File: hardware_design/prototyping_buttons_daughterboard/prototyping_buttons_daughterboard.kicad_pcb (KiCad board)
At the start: 2 copper layers, 80 x 30.5 mm, 10 parts, among them J1 Conn_02x10_Counter_Clockwise, J2 Conn_02x10_Counter_Clockwise

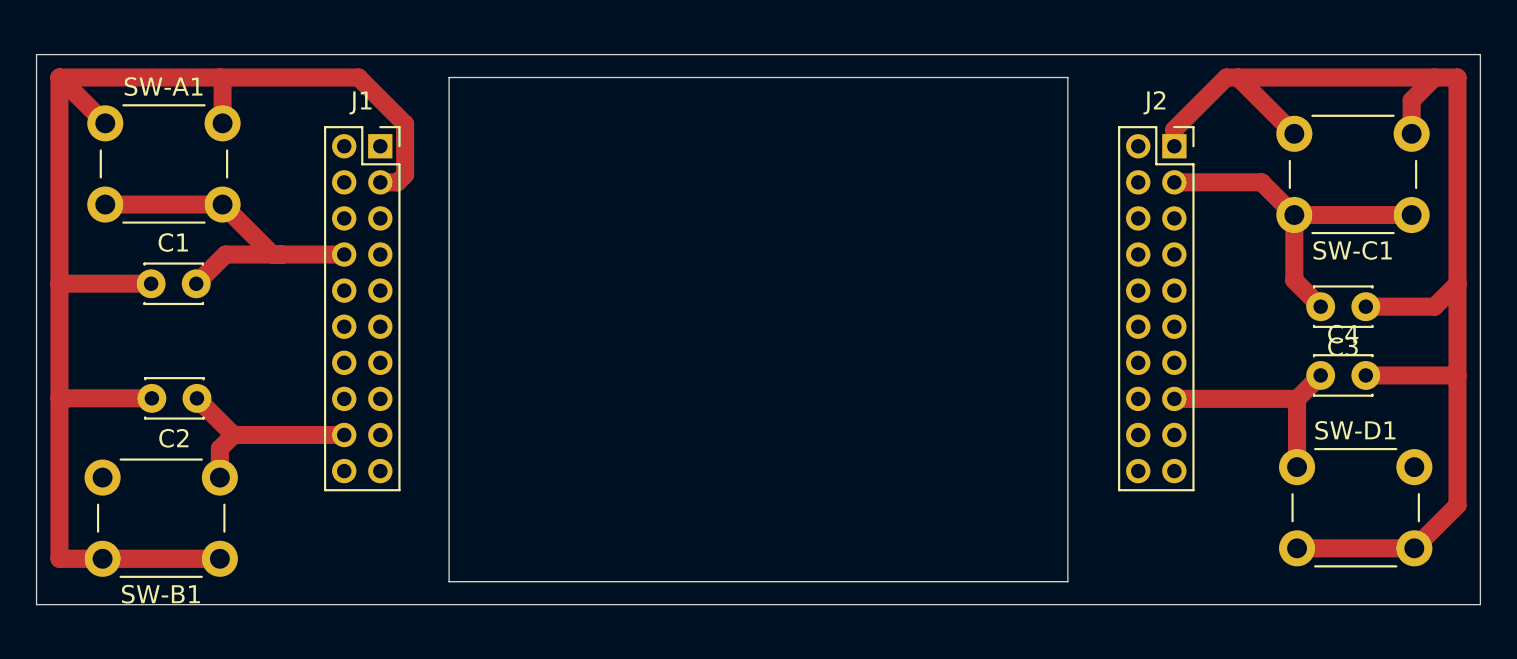
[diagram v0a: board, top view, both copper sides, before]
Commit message: Commit fixes issues with board design as raised in #3.
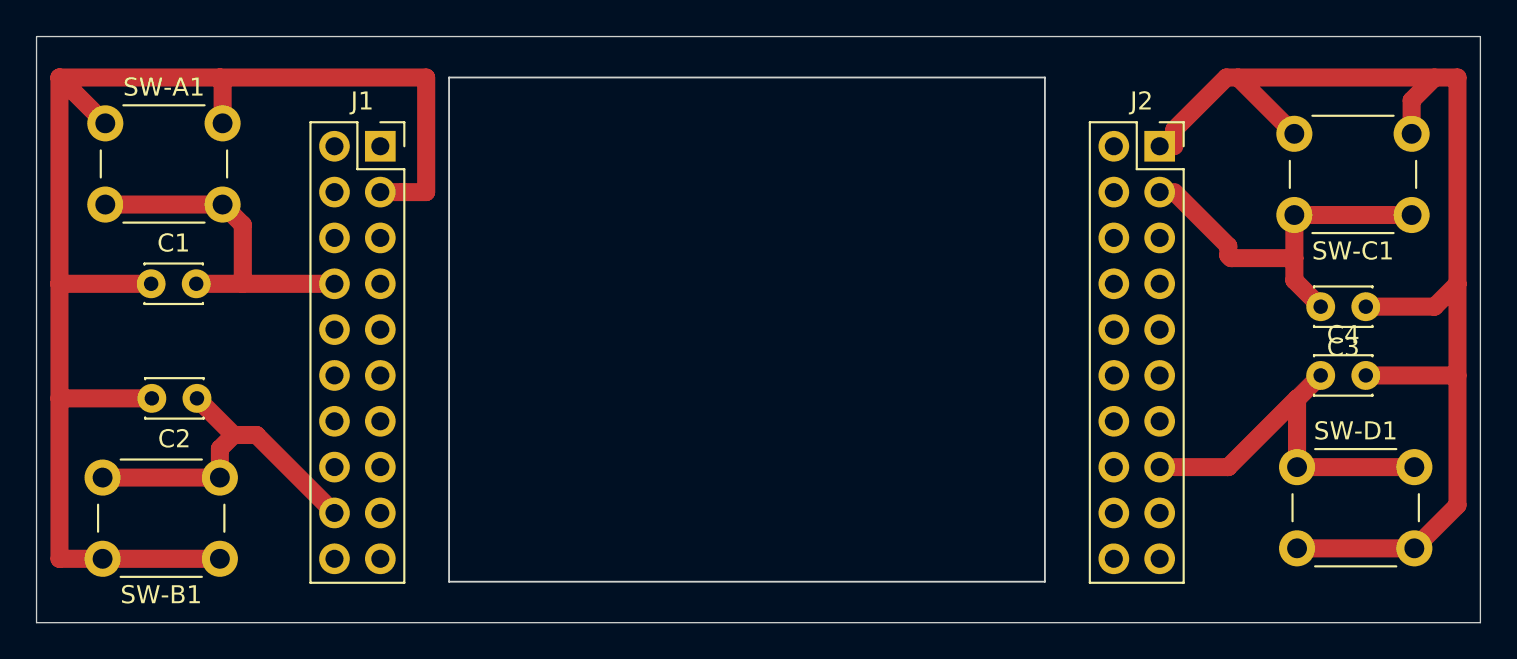
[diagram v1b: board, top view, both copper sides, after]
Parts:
- J1, J2: footprint Connector_PinSocket_2.00mm:PinSocket_2x10_P2.00mm_Vertical -> Connector_PinSocket_2.54mm:PinSocket_2x10_P2.54mm_Vertical
- moved J2 0.81 mm to (129.5, 53.3)
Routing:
- net Net-(C4-Pad1): track 12.5 -> 20.5 mm
- net Net-(C2-Pad1): track 11.7 -> 19.4 mm
- net Net-(C1-Pad1): track 76.5 -> 81.2 mm
- net Net-(C3-Pad2): track 19.6 -> 20.7 mm
- net Net-(C1-Pad2): track 19.8 -> 19.0 mm
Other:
- board size 80 x 30.5 mm -> 80 x 32.5 mm
